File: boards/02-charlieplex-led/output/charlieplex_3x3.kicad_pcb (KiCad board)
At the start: 2 copper layers, 50 x 55 mm, 14 parts, among them U1 MCU

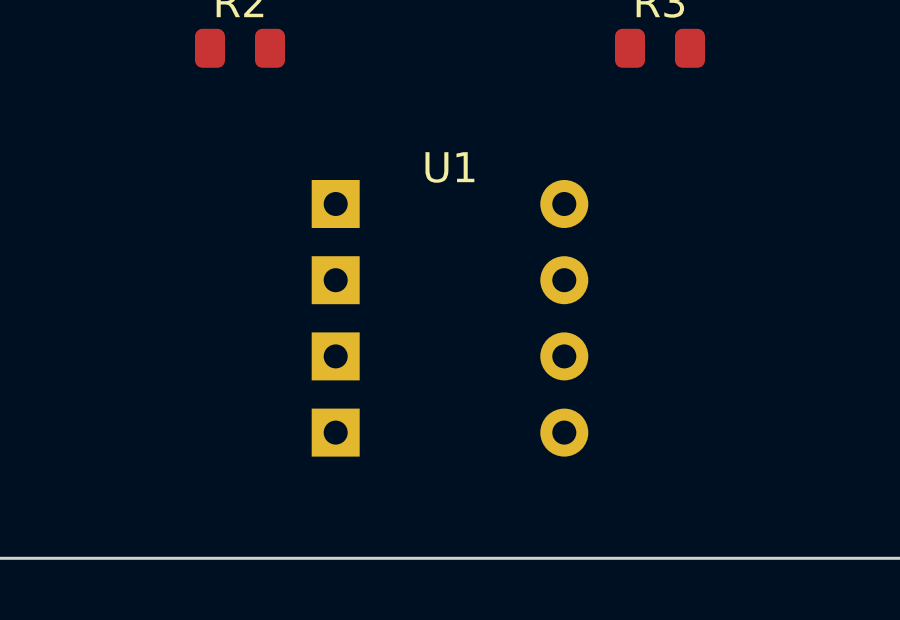
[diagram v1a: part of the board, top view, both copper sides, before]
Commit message: fix(board-02): align U1 pads to 0.1mm grid + switch to kct route subprocess
The charlieplex test board (board 02) was at 9/10 nets routed with 8
pad-grid DRC warnings and no manufacturing bundle.  Two coupled changes
restore the gold-standard end-state and unblock the milestone-B route.

1. **U1 pad-grid alignment** (clears the 8 pad-grid warnings)

   The synthetic DIP-8 footprint was using strict imperial dimensions
   (7.62mm row spacing, 2.54mm pin pitch) which cannot place both
   pad rows on the router's 0.1mm grid simultaneously -- 7.62 mod 0.1
   = 0.02, so the two rows necessarily land on opposite sides of the
   nearest grid line.

   Replace with grid-friendly dimensions (7.6mm row spacing, 2.5mm
   pin pitch) and apply a 0.05mm y_offset so that ``(i - 1.5) * pitch``
   half-integer multiples also land on the grid.  All eight pads now
   sit at integer multiples of 0.1mm.  The schematic symbol is the
   generic ``Conn_01x08`` (the DIP-8 is a synthetic stand-in for an
   MCU), so the ≤0.04mm geometric shift has no manufacturing or
   schematic-net consequence.

2. **Switch route step to ``kct route`` subprocess** (closes the
   NODE_x net gap and the GND completion gap)

   The legacy in-process ``router.route_all()`` regressed on this
   board with current router code -- all four charlieplex NODE_x nets
   now fail with ``BLOCKED_BY_COMPONENT: Path blocked by component
   keepout`` even though the previously-committed routed PCB had them
   all connected.  ``route_all_negotiated`` (the PR #3034 board 01
   pattern) fares slightly better but still produces 22+ sub-0.127mm
   clearance violations.

   ``kct route --strategy negotiated --iterations 30`` is the only
   recipe that yields 10/10 nets DRC-clean on this geometry.  Mirrors
   PR #2981 (board 05) and PR #2991 (board 07) subprocess pattern.
   ``kct route`` also auto-pours zones for GND/VCC after routing, so
   the 3 GND pads and the lone VCC pad reach ``status=complete`` via
   plane connectivity w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
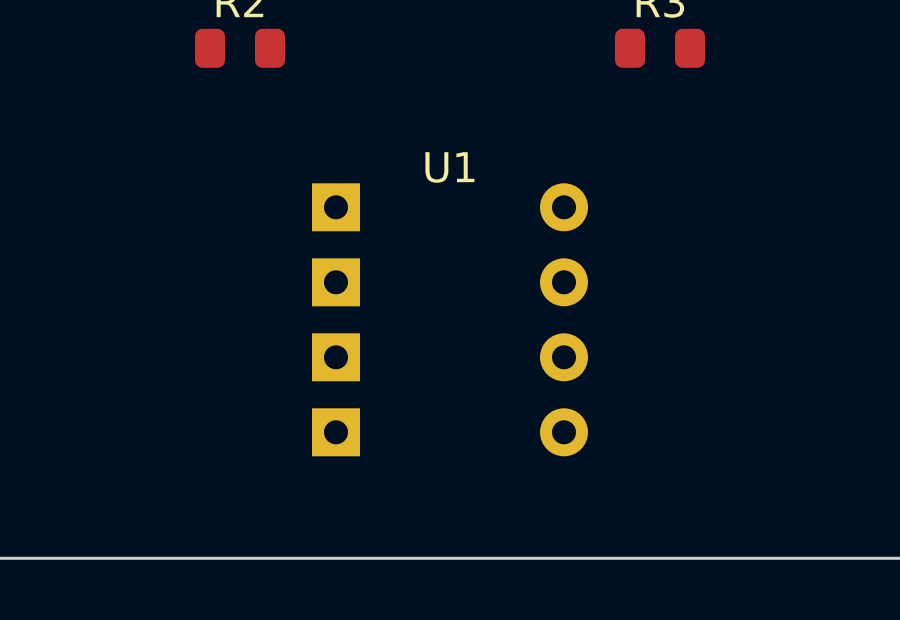
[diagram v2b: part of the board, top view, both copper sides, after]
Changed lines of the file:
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@@
       (effects (font (size 1 1) (thickness 0.15)))
     )
-    (pad "1" thru_hole rect (at -3.810 -3.810) (size 1.6 1.6) (drill 0.8) (layers "*.Cu" "*.Mask") (net 1 "LINE_A"))
-    (pad "2" thru_hole rect (at -3.810 -1.270) (size 1.6 1.6) (drill 0.8) (layers "*.Cu" "*.Mask") (net 2 "LINE_B"))
-    (pad "3" thru_hole rect (at -3.810 1.270) (size 1.6 1.6) (drill 0.8) (layers "*.Cu" "*.Mask") (net 3 "LINE_C"))
-    (pad "4" thru_hole rect (at -3.810 3.810) (size 1.6 1.6) (drill 0.8) (layers "*.Cu" "*.Mask") (net 4 "LINE_D"))
-    (pad "5" thru_hole oval (at 3.810 3.810) (size 1.6 1.6) (drill 0.8) (layers "*.Cu" "*.Mask") (net 10 "GND"))
-    (pad "6" thru_hole oval (at 3.810 1.270) (size 1.6 1.6) (drill 0.8) (layers "*.Cu" "*.Mask") (net 10 "GND"))
-    (pad "7" thru_hole oval (at 3.810 -1.270) (size 1.6 1.6) (drill 0.8) (layers "*.Cu" "*.Mask") (net 9 "VCC"))
-    (pad "8" thru_hole oval (at 3.810 -3.810) (size 1.6 1.6) (drill 0.8) (layers "*.Cu" "*.Mask") (net 10 "GND"))
+    (pad "1" thru_hole rect (at -3.800 -3.700) (size 1.6 1.6) (drill 0.8) (layers "*.Cu" "*.Mask") (net 1 "LINE_A"))
+    (pad "2" thru_hole rect (at -3.800 -1.200) (size 1.6 1.6) (drill 0.8) (layers "*.Cu" "*.Mask") (net 2 "LINE_B"))
+    (pad "3" thru_hole rect (at -3.800 1.300) (size 1.6 1.6) (drill 0.8) (layers "*.Cu" "*.Mask") (net 3 "LINE_C"))
+    (pad "4" thru_hole rect (at -3.800 3.800) (size 1.6 1.6) (drill 0.8) (layers "*.Cu" "*.Mask") (net 4 "LINE_D"))
+    (pad "5" thru_hole oval (at 3.800 3.800) (size 1.6 1.6) (drill 0.8) (layers "*.Cu" "*.Mask") (net 10 "GND"))
+    (pad "6" thru_hole oval (at 3.800 1.300) (size 1.6 1.6) (drill 0.8) (layers "*.Cu" "*.Mask") (net 10 "GND"))
+    (pad "7" thru_hole oval (at 3.800 -1.200) (size 1.6 1.6) (drill 0.8) (layers "*.Cu" "*.Mask") (net 9 "VCC"))
+    (pad "8" thru_hole oval (at 3.800 -3.700) (size 1.6 1.6) (drill 0.8) (layers "*.Cu" "*.Mask") (net 10 "GND"))
   )
   (footprint "Resistor_SMD:R_0805_2012Metric"
